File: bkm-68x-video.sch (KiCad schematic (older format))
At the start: 71 parts, among them J1 PR_R, J10 TP_VIDEO_OE, J11 TP_VSYNC, J13 PR_R_OUT, J15 Y_G_OUT, J16 PB_B_OUT, J17 EXT_SYNC_OUT, J2 Y_G, J3 PB_B, J4 EXT_SYNC, J5 TP_Y_G, J6 TP_PB_B, J7 TP_PR_R, J8 TP_HSYNC, J9 TP_INT_EXT_SYNC, Q1 MMBT3904, SW3 PR_R_TERM, SW4 Y_G_TERM, SW5 PB_B_TERM, SW6 EXT_SYNC_TERM, U1 ADG1611BCPZ, U16 SN74LVC1G14DBV, U17 ISL4089, U2 THS7374, U3 ISL59885, U4 ADG734, U8 TC7WH125

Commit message: Rev. F1
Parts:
- removed U4: ADG734, Package_SO:TSSOP-20_4.4x6.5mm_P0.65mm, symbol adg734:ADG734
- added D10, D9: NM, Diode_SMD:D_SOD-123, symbol bkm-68x-simple-rescue:D_Small_ALT
- added J14: VSYNC_DISCRETE, BNC-THT:BNC-THT, symbol bkm-68x-simple-rescue:Conn_Coaxial
- added Q2: MMBT3904, Package_TO_SOT_SMD:SOT-23_Handsoldering, symbol Device:Q_NPN_BEC
- added R6: 75R, Resistor_SMD:R_0805_2012Metric_Pad1.20x1.40mm_HandSolder, symbol bkm-68x-simple-rescue:R
- added R7: 1K, Resistor_SMD:R_0805_2012Metric_Pad1.20x1.40mm_HandSolder, symbol bkm-68x-simple-rescue:R
- added R8: 10K, Resistor_SMD:R_0805_2012Metric_Pad1.20x1.40mm_HandSolder, symbol bkm-68x-simple-rescue:R
- added U301: FSA2257MUX, Package_SO:MSOP-10_3x3mm_P0.5mm, symbol FSA2257:FSA2257MUX
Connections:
- net +5VA: now also C9.1, D9.1 (K), R7.1, U301.3 (VCC), U301.3 (VCC); no longer C9.2
- net EXT_SYNC_AMP: now also U301.6 (1B1)
- net GND: now also C9.2, D10.2 (A), J14.2 (Ext), Q2.2 (E), R6.2, U301.8 (GND), U301.8 (GND); no longer C9.1
- net INT_~EXT~_SYNC: now also U301.7 (1S)
- net NORM_Y_G: now also U301.2 (2S)
- net SYNC_SRC: now also U301.4 (1A)
- net Y_G_AMP: now also U301.1 (2B1), U301.5 (1B0)
- net Y_G_NORM: now also U301.10 (2B0)
- net Y_G_SW: now also U301.9 (2A)
- new net: D10.1 (K), D9.2 (A), J14.1 (In), R6.1, R8.1
- new net: Q2.1 (B), R8.2
- new net VSYNC_DISCRETE_IN: Q2.3 (C), R7.2
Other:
- moved on the sheet: C1, C10, C11, C13, C2, C27, C3, C4, C5, C54, C55, C6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

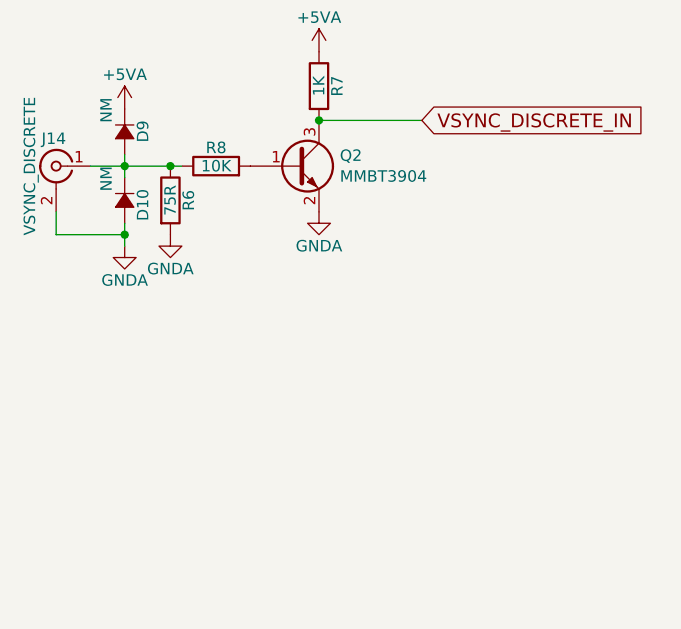
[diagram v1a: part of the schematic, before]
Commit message: Added vsync out
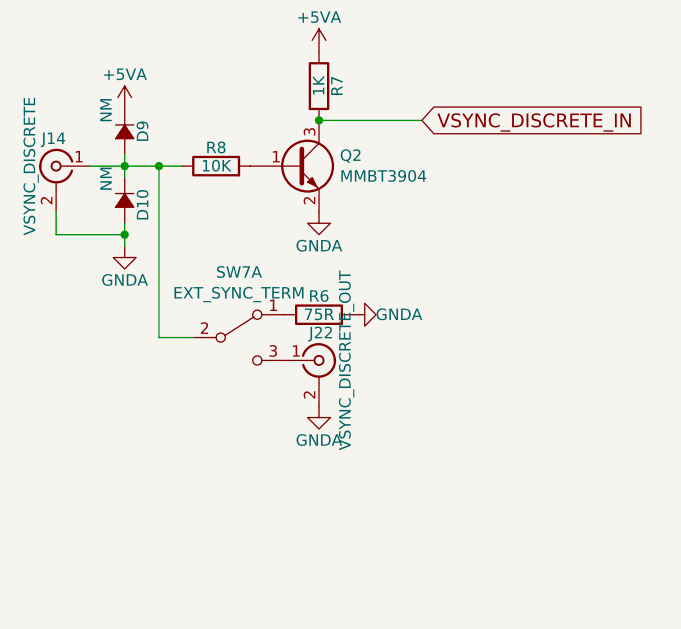
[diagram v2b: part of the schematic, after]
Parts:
- added J22: VSYNC_DISCRETE_OUT, BNC-THT:BNC-THT, symbol bkm-68x-simple-rescue:Conn_Coaxial
- added SW7: EXT_SYNC_TERM, JS202011SCQN:JS202011SCQN, symbol Switch:SW_DPDT_x2
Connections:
- net GND: now also J22.2 (Ext)
- net at D10.1 (K), D9.2 (A), J14.1 (In)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: now also SW7.2 (B); no longer R6.1
- new net: J22.1 (In), SW7.3 (C)
- new net: R6.1, SW7.1 (A)
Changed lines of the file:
@@
 	1200 5450 1200 5500
-Wire Wire Line
-	1200 5450 1400 5450
 Wire Wire Line
 	1200 5750 1200 5800
@@
 $EndComp
 $Comp
-L bkm-68x-simple-rescue:R R6
-U 1 1 62148AFE
-P 1400 5600
-F 0 "R6" V 1480 5600 50  0000 C CNN
-F 1 "75R" V 1400 5600 50  0000 C CNN
-F 2 "Resistor_SMD:R_0805_2012Metric_Pad1.20x1.40mm_HandSolder" V 1330 5600 50  0001 C CNN
-F 3 "" H 1400 5600 50  0001 C CNN
-	1    1400 5600
-	1    0    0    -1
-$EndComp
-Connection ~ 1400 5450
-Wire Wire Line
-	1400 5450 1450 5450
-$Comp
-L power:GNDA #PWR0306
-U 1 1 62149B83
-P 1400 5750
-F 0 "#PWR0306" H 1400 5500 50  0001 C CNN
-F 1 "GNDA" H 1400 5600 50  0000 C CNN
-F 2 "" H 1400 5750 50  0001 C CNN
-F 3 "" H 1400 5750 50  0001 C CNN
-	1    1400 5750
-	1    0    0    -1
-$EndComp
-$Comp
 L Device:Q_NPN_BEC Q2
 U 1 1 6238F86F
@@
 Wire Wire Line
 	2550 8100 2600 8100
+$Comp
+L bkm-68x-simple-rescue:Conn_Coaxial J22
+U 1 1 626F8642
+P 2050 6300
+F 0 "J22" H 2060 6420 50  0000 C CNN
+F 1 "VSYNC_DISCRETE_OUT" V 2165 6300 50  0000 C CNN
+F 2 "BNC-THT:BNC-THT" H 2050 6300 50  0001 C CNN
+F 3 "" H 2050 6300 50  0001 C CNN
+	1    2050 6300
+	1    0    0    -1
+$EndComp
+$Comp
+L power:GNDA #PWR0151
+U 1 1 626F8648
+P 2050 6500
+F 0 "#PWR0151" H 2050 6250 50  0001 C CNN
+F 1 "GNDA" H 2050 6350 50  0000 C CNN
+F 2 "" H 2050 6500 50  0001 C CNN
+F 3 "" H 2050 6500 50  0001 C CNN
+	1    2050 6500
+	1    0    0    -1
+$EndComp
+$Comp
+L power:GNDA #PWR0152
+U 1 1 626F864E
+P 2200 6100
+F 0 "#PWR0152" H 2200 5850 50  0001 C CNN
+F 1 "GNDA" V 2200 5900 50  0000 C CNN
+F 2 "" H 2200 6100 50  0001 C CNN
+F 3 "" H 2200 6100 50  0001 C CNN
+	1    2200 6100
+	0    -1   -1   0
+$EndComp
+$Comp
+L Switch:SW_DPDT_x2 SW7
+U 1 1 626F8655
+P 1700 6200
+F 0 "SW7" H 1700 6485 50  0000 C CNN
+F 1 "EXT_SYNC_TERM" H 1700 6394 50  0000 C CNN
+F 2 "JS202011SCQN:JS202011SCQN" H 1700 6200 50  0001 C CNN
+F 3 "~" H 1700 6200 50  0001 C CNN
+	1    1700 6200
+	1    0    0    -1
+$EndComp
+$Comp
+L bkm-68x-simple-rescue:R R6
+U 1 1 626F865B
+P 2050 6100
+F 0 "R6" V 2130 6100 50  0000 C CNN
+F 1 "75R" V 2050 6100 50  0000 C CNN
+F 2 "Resistor_SMD:R_0805_2012Metric_Pad1.20x1.40mm_HandSolder" V 1980 6100 50  0001 C CNN
+F 3 "" H 2050 6100 50  0001 C CNN
+	1    2050 6100
+	0    -1   -1   0
+$EndComp
+Wire Wire Line
+	1200 5450 1350 5450
+Wire Wire Line
+	1350 5450 1350 6200
+Wire Wire Line
+	1350 6200 1500 6200
+Connection ~ 1350 5450
+Wire Wire Line
+	1350 5450 1450 5450
 $EndSCHEMATC

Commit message: Rev. F2
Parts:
- C1, C10, C13, C2, C27, C3, C4, C5, C6, C62, C63, C64, C7, C9: JLC (none) -> 0805; LCSC (none) -> C77082
- C11: JLC (none) -> 0805; LCSC (none) -> C107156
- C54: JLC (none) -> 0805; LCSC (none) -> C1790
- C55: JLC (none) -> 0805; LCSC (none) -> C76630
- C65: JLC (none) -> 0805; LCSC (none) -> C107112
- Q1, Q2: JLC (none) -> SOT-23(SOT-23-3); LCSC (none) -> C94514
- R1, R10, R12, R14, R2, R3, R4, R6: JLC (none) -> 0805; LCSC (none) -> C141697
- R11, R13, R9: JLC (none) -> 0805; LCSC (none) -> C114523
- R7: JLC (none) -> 0805; LCSC (none) -> C95781
- R71, R72: JLC (none) -> 0805; LCSC (none) -> C114541
- R8, R81, R84: JLC (none) -> 0805; LCSC (none) -> C84376
- R80: JLC (none) -> 0805; LCSC (none) -> C105577
- R90: JLC (none) -> 0805; LCSC (none) -> C100045
- SW3, SW4, SW5, SW6, SW7: JLC (none) -> SMD; LCSC (none) -> C223858
- U1: JLC (none) -> QFN-16(4x4); LCSC (none) -> C2673366
- U16: JLC (none) -> SOT-23-5; LCSC (none) -> C434069
- U2: JLC (none) -> TSSOP-14; LCSC (none) -> C2652746
- U3: JLC (none) -> SOIC-8; LCSC (none) -> C1519107
- U8: JLC (none) -> TSSOP-8; LCSC (none) -> C554358

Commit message: Rev. F4
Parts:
- added C30, C31, C32: NM, Capacitor_SMD:C_0805_2012Metric_Pad1.18x1.45mm_HandSolder, symbol bkm-68x-simple-rescue:C_Small
- added C33: 22pF, Capacitor_SMD:C_0805_2012Metric_Pad1.18x1.45mm_HandSolder, symbol bkm-68x-simple-rescue:C_Small
- added R44: 1K, Resistor_SMD:R_0805_2012Metric_Pad1.20x1.40mm_HandSolder, symbol bkm-68x-simple-rescue:R
- added U501: ADG1611, Package_SO:TSSOP-16_4.4x5mm_P0.65mm, symbol adg1611:ADG1611
- U16: LCSC C434069 -> C7835
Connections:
- net +5VA: now also U501.13 (VDD), U501.13 (VDD), U501.13 (VDD), U501.13 (VDD)
- net -5VA: now also U501.4 (VSS), U501.4 (VSS), U501.4 (VSS), U501.4 (VSS)
- net GND: now also C30.2, C31.2, C32.2, C33.1, U501.11 (S), U501.5 (GND), U501.5 (GND), U501.5 (GND), U501.5 (GND), U501.9 (IN)
- net PB_B: now also U501.7 (D)
- net PB_B_AMP: now also C32.1
- net PR_R: now also U501.14 (S)
- net PR_R_AMP: now also C30.1
- net Y_G: now also U501.2 (D)
- net Y_G_AMP: now also C33.2
- net Y_G_SW: now also C31.1
- net ~CSYNC: now also R44.1; no longer U16.4
- net ~VIDEO_OE: now also U501.1 (IN), U501.16 (IN), U501.8 (IN)
- net PR_R_L: now reaches R10.2, R9.2, U1.13 (D)
- net PR_R_L: now also U501.15 (D)
- net Y_G_L: now reaches R11.2, R12.2, U1.1 (S)
- net Y_G_L: now also U501.3 (S)
- net PB_B_L: now reaches R13.2, R14.2, U1.4 (S)
- net PB_B_L: now also U501.6 (S)
- new net: R44.2, U16.4
- no-connect marks 0 -> 2
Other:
- note added: "Only U1 or U501 should be mounted.\nADG1611BRUZ is pin-compatible with DG1411-EEQ-T1-GE4\nADG1611BCPZ is pin-compatible with DG1411-EEN-T1-GE4"
